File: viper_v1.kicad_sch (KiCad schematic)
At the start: 24 parts, among them SW1 SW_Push, SW2 SW_Push, SW3 SW_Push, SW4 SW_Push, SW5 SW_Push, U1 ATmega32U4-A, Y1 16MHz

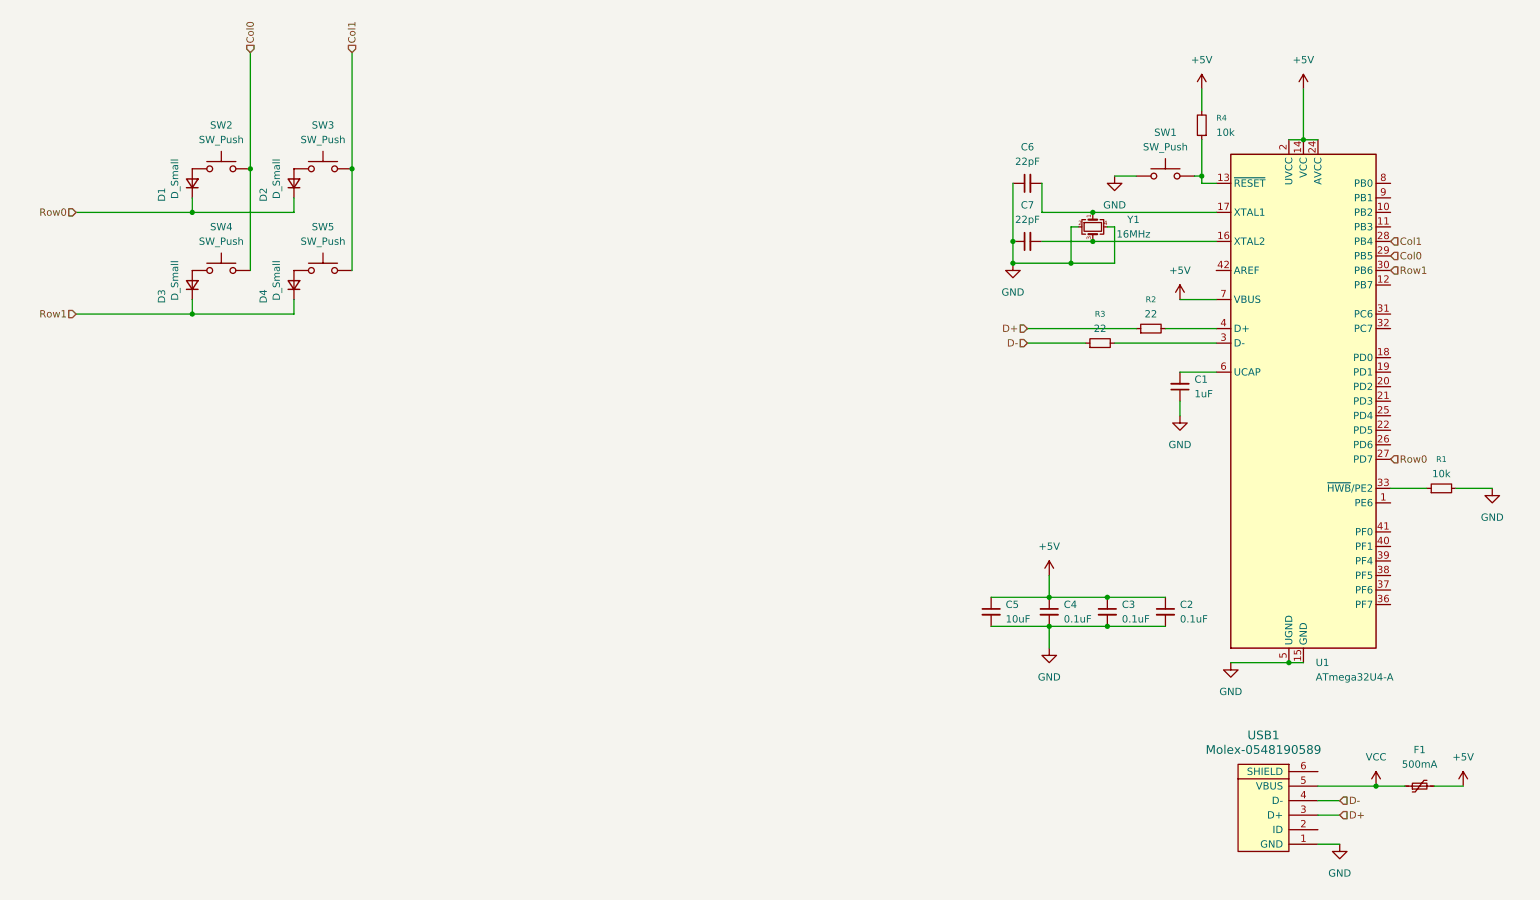
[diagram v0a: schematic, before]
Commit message: Assigned footprints
Updated/reannotated schematic

init pcb with viper outline

Add ISP header
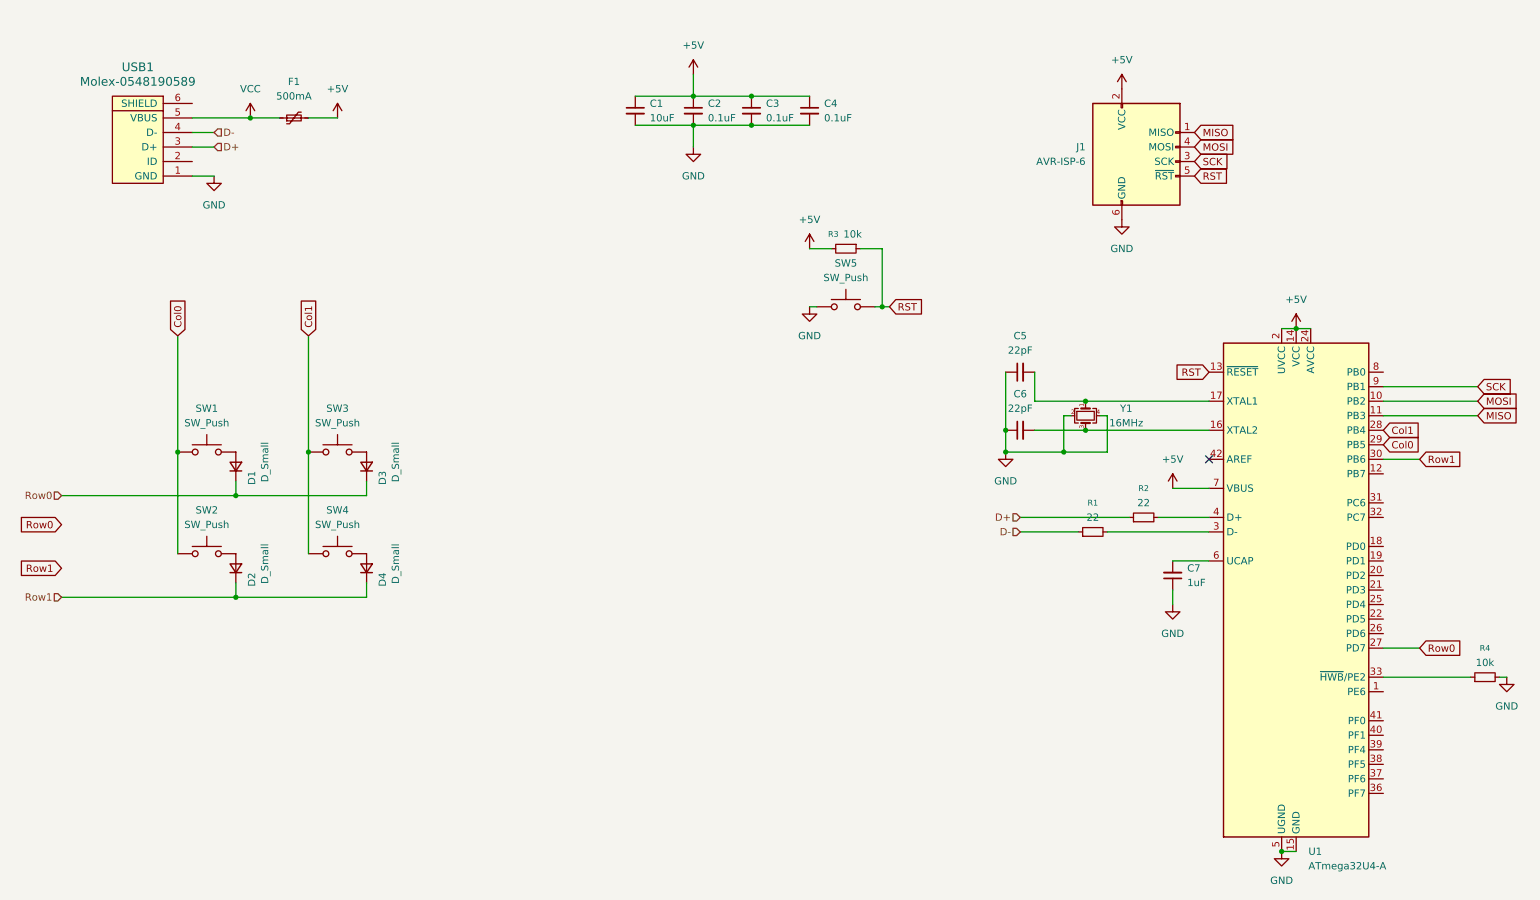
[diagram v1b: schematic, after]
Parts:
- removed SW5: SW_Push, symbol Switch:SW_Push
- added J1: AVR-ISP-6, random-keyboard-parts:Reset_Pretty-Mask, symbol Connector:AVR-ISP-6
- added SW1: SW_Push, MX_Solderable:MX-Solderable-1U, symbol Switch:SW_Push
- C1: renamed from C5; footprint (none) -> Capacitor_SMD:C_0805_2012Metric
- C2: renamed from C4; footprint (none) -> Capacitor_SMD:C_0805_2012Metric
- C3: footprint (none) -> Capacitor_SMD:C_0805_2012Metric
- C4: renamed from C2; footprint (none) -> Capacitor_SMD:C_0805_2012Metric
- C5: renamed from C6; footprint (none) -> Capacitor_SMD:C_0805_2012Metric
- C6: renamed from C7; footprint (none) -> Capacitor_SMD:C_0805_2012Metric
- C7: renamed from C1; footprint (none) -> Capacitor_SMD:C_0805_2012Metric
- D1, D2, D3, D4: footprint (none) -> Diode_SMD:D_SOD-123
- F1: footprint (none) -> Fuse:Fuse_1206_3216Metric
- R1: renamed from R3; footprint (none) -> Resistor_SMD:R_0805_2012Metric
- R2: footprint (none) -> Resistor_SMD:R_0805_2012Metric
- R3: renamed from R4; footprint (none) -> Resistor_SMD:R_0805_2012Metric
- R4: renamed from R1; footprint (none) -> Resistor_SMD:R_0805_2012Metric
- SW2, SW3, SW4: footprint (none) -> MX_Solderable:MX-Solderable-1U
- SW5: renamed from SW1; footprint (none) -> random-keyboard-parts:SKQG-1155865
- USB1: footprint (none) -> random-keyboard-parts:Molex-0548190589
- Y1: footprint (none) -> Crystal:Crystal_SMD_3225-4Pin_3.2x2.5mm
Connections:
- net +5V: now also J1.2 (VCC)
- net Col0: now also SW2.1, SW1.1; no longer SW2.2, SW4.2
- net Col1: now also SW3.1, SW4.1; no longer SW3.2
- net GND: now also J1.6 (GND)
- net Row0: now also D3.1 (K); no longer D2.1 (K)
- net Row1: now also D2.1 (K); no longer D3.1 (K)
- net RST: now reaches R3.1, SW5.2, U1.13 (~{RESET})
- net RST: now also J1.5 (~{RST})
- net at D1.2 (A): now also SW1.2; no longer SW2.1
- net at D4.2 (A): now also SW4.2
- net at D2.2 (A): now also SW2.2; no longer SW3.1
- net MOSI: now reaches U1.10 (PB2)
- net MOSI: now also J1.4 (MOSI)
- net MISO: now reaches U1.11 (PB3)
- net MISO: now also J1.1 (MISO)
- net SCK: now reaches U1.9 (PB1)
- net SCK: now also J1.3 (SCK)
- net at D3.2 (A): now also SW3.2; no longer SW4.1
- no-connect marks 0 -> 1
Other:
- moved on the sheet: C1, C2, C3, C4, C5, C6, C7, F1, R1, R2, R3, R4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

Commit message: Added rows/columns for simple wkl layout
Added values to keys in schematic & updated meta keys

Aligned switches & diodes

Moved some footprints around to prevent overlapping.

Added PWR Flags & connected shield

Custom SKQG footprint.

Set up 15mil power netclass for +5V, VCC & GND
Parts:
- removed D2: D_Small, Diode_SMD:D_SOD-123, symbol Device:D_Small
- removed SW2: SW_Push, MX_Solderable:MX-Solderable-1U, symbol Switch:SW_Push
- added D10, D11, D12, D13, D14, D15, D16, D17, D18, D19, D20, D21, D22, D23, D24, D25, D26, D27, D28, D29, D3, D30, D31, D32, D33, D34, D35, D36, D37, D38, D39, D40, D41, D42, D43, D44, D45, D46, D47, D48, D49, D5, D50, D51, D52, D53, D54, D55, D56, D57, D58, D6, D7, D8, D9: D_Small, Diode_SMD:D_SOD-123, symbol Device:D_Small
- added SW10: KC_9, MX_Solderable:MX-Solderable-1U, symbol Switch:SW_Push
- added SW11: KC_0, MX_Solderable:MX-Solderable-1U, symbol Switch:SW_Push
- added SW12: KC_MINS, MX_Solderable:MX-Solderable-1U, symbol Switch:SW_Push
- added SW13: KC_EQL, MX_Solderable:MX-Solderable-1U, symbol Switch:SW_Push
- added SW14: KC_BSPC, MX_Solderable:MX-Solderable-2U, symbol Switch:SW_Push
- added SW15: KC_TAB, MX_Solderable:MX-Solderable-1.5U, symbol Switch:SW_Push
- added SW16: KC_Q, MX_Solderable:MX-Solderable-1U, symbol Switch:SW_Push
- added SW17: KC_W, MX_Solderable:MX-Solderable-1U, symbol Switch:SW_Push
- added SW18: KC_E, MX_Solderable:MX-Solderable-1U, symbol Switch:SW_Push
- added SW19: KC_R, MX_Solderable:MX-Solderable-1U, symbol Switch:SW_Push
- added SW20: KC_T, MX_Solderable:MX-Solderable-1U, symbol Switch:SW_Push
- added SW21: KC_Y, MX_Solderable:MX-Solderable-1U, symbol Switch:SW_Push
- added SW22: KC_U, MX_Solderable:MX-Solderable-1U, symbol Switch:SW_Push
- added SW23: KC_I, MX_Solderable:MX-Solderable-1U, symbol Switch:SW_Push
- added SW24: KC_O, MX_Solderable:MX-Solderable-1U, symbol Switch:SW_Push
- added SW25: KC_P, MX_Solderable:MX-Solderable-1U, symbol Switch:SW_Push
- added SW26: KC_LBRC, MX_Solderable:MX-Solderable-1U, symbol Switch:SW_Push
- added SW27: KC_RBRC, MX_Solderable:MX-Solderable-1U, symbol Switch:SW_Push
- added SW28: KC_BSLS, MX_Solderable:MX-Solderable-1.5U, symbol Switch:SW_Push
- added SW29: KC_CAPS, MX_Solderable:MX-Solderable-1.75U, symbol Switch:SW_Push
- added SW3: KC_2, MX_Solderable:MX-Solderable-1U, symbol Switch:SW_Push
- added SW30: KC_A, MX_Solderable:MX-Solderable-1U, symbol Switch:SW_Push
- added SW31: KC_S, MX_Solderable:MX-Solderable-1U, symbol Switch:SW_Push
- added SW32: KC_D, MX_Solderable:MX-Solderable-1U, symbol Switch:SW_Push
- added SW33: KC_F, MX_Solderable:MX-Solderable-1U, symbol Switch:SW_Push
- added SW34: KC_G, MX_Solderable:MX-Solderable-1U, symbol Switch:SW_Push
- added SW35: KC_H, MX_Solderable:MX-Solderable-1U, symbol Switch:SW_Push
- added SW36: KC_J, MX_Solderable:MX-Solderable-1U, symbol Switch:SW_Push
- added SW37: KC_K, MX_Solderable:MX-Solderable-1U, symbol Switch:SW_Push
- added SW38: KC_L, MX_Solderable:MX-Solderable-1U, symbol Switch:SW_Push
- added SW39: KC_SCLN, MX_Solderable:MX-Solderable-1U, symbol Switch:SW_Push
- added SW40: KC_QUOT, MX_Solderable:MX-Solderable-1U, symbol Switch:SW_Push
- added SW41: KC_ENT, MX_Solderable:MX-Solderable-2.25U-ReversedStabilizers, symbol Switch:SW_Push
- added SW42: KC_LSFT, MX_Solderable:MX-Solderable-2.25U-ReversedStabilizers, symbol Switch:SW_Push
- added SW43: KC_Z, MX_Solderable:MX-Solderable-1U, symbol Switch:SW_Push
- added SW44: KC_X, MX_Solderable:MX-Solderable-1U, symbol Switch:SW_Push
- added SW45: KC_C, MX_Solderable:MX-Solderable-1U, symbol Switch:SW_Push
- added SW46: KC_V, MX_Solderable:MX-Solderable-1U, symbol Switch:SW_Push
- added SW47: KC_B, MX_Solderable:MX-Solderable-1U, symbol Switch:SW_Push
- added SW48: KC_N, MX_Solderable:MX-Solderable-1U, symbol Switch:SW_Push
- added SW49: KC_M, MX_Solderable:MX-Solderable-1U, symbol Switch:SW_Push
- added SW50: KC_COMM, MX_Solderable:MX-Solderable-1U, symbol Switch:SW_Push
- added SW51: KC_DOT, MX_Solderable:MX-Solderable-1U, symbol Switch:SW_Push
- added SW52: KC_SLSH, MX_Solderable:MX-Solderable-1U, symbol Switch:SW_Push
- added SW53: KC_RSFT, MX_Solderable:MX-Solderable-2.75U-ReversedStabilizers, symbol Switch:SW_Push
- added SW54: KC_LEFT_GUI, MX_Solderable:MX-Solderable-1U, symbol Switch:SW_Push
- added SW55: KC_LEFT_ALT, MX_Solderable:MX-Solderable-1.5U, symbol Switch:SW_Push
- added SW56: KC_SPACE, MX_Solderable:MX-Solderable-7U-ReversedStabilizers, symbol Switch:SW_Push
- added SW57: KC_RIGHT_GUI, MX_Solderable:MX-Solderable-1U, symbol Switch:SW_Push
- added SW58: KC_RIGHT_ALT, MX_Solderable:MX-Solderable-1.5U, symbol Switch:SW_Push
- added SW59: SW_RESET, random-keyboard-parts:SKQG-1155865, symbol Switch:SW_Push
- added SW6: KC_5, MX_Solderable:MX-Solderable-1U, symbol Switch:SW_Push
- added SW7: KC_6, MX_Solderable:MX-Solderable-1U, symbol Switch:SW_Push
- added SW8: KC_7, MX_Solderable:MX-Solderable-1U, symbol Switch:SW_Push
- added SW9: KC_8, MX_Solderable:MX-Solderable-1U, symbol Switch:SW_Push
- SW1: value SW_Push -> KC_GRV
- SW2: renamed from SW3; value SW_Push -> KC_1
- SW4: value SW_Push -> KC_3
- SW5: value SW_Push -> KC_4; footprint random-keyboard-parts:SKQG-1155865 -> MX_Solderable:MX-Solderable-1U
- renumbered D3 to D2, R3 to R1, R1 to R3
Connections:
- net Col0: now also U1.28 (PB4), SW15.1, SW29.1, SW42.1; no longer U1.29 (PB5)
- net Col1: now also U1.29 (PB5), SW16.1, SW30.1, SW54.1; no longer SW4.1, U1.28 (PB4)
- net GND: now also USB1.6 (SHIELD), SW59.1; no longer SW5.1
- net RST: now also SW59.2; no longer SW5.2
- net Row0: now also D4.1 (K), U1.1 (PE6), D10.1 (K), D11.1 (K), D12.1 (K), D13.1 (K), D14.1 (K), D3.1 (K), D5.1 (K), D6.1 (K), D7.1 (K), D8.1 (K), D9.1 (K); no longer U1.27 (PD7)
- net Row1: now also U1.38 (PF5), D15.1 (K), D16.1 (K), D17.1 (K), D18.1 (K), D19.1 (K), D20.1 (K), D21.1 (K), D22.1 (K), D23.1 (K), D24.1 (K), D25.1 (K), D26.1 (K), D27.1 (K), D28.1 (K); no longer D4.1 (K), U1.30 (PB6)
- net XTAL1: now reaches C5.2, U1.17 (XTAL1), Y1.1
- net XTAL2: now reaches C6.2, U1.16 (XTAL2), Y1.3
- net Col8: now reaches U1.19 (PD1)
- net Col8: now also SW23.1, SW37.1, SW49.1, SW9.1
- net Col9: now reaches U1.20 (PD2)
- net Col9: now also SW10.1, SW24.1, SW38.1, SW50.1
- net Col10: now reaches U1.21 (PD3)
- net Col10: now also SW11.1, SW25.1, SW39.1, SW51.1, SW57.1
- net Col11: now reaches U1.22 (PD5)
- net Col11: now also SW12.1, SW26.1, SW40.1, SW52.1, SW58.1
- net Col12: now reaches U1.25 (PD4)
- net Col12: now also SW13.1, SW27.1
- net Col13: now reaches U1.26 (PD6)
- net Col13: now also SW14.1, SW28.1, SW41.1, SW53.1
- net Col3: now reaches U1.31 (PC6)
- net Col3: now also SW4.1, SW18.1, SW32.1, SW44.1
- net Col4: now reaches U1.32 (PC7)
- net Col4: now also SW5.1, SW19.1, SW33.1, SW45.1
- net Col6: now reaches U1.36 (PF7)
- net Col6: now also SW21.1, SW35.1, SW47.1, SW56.1, SW7.1
- net Col5: now reaches U1.37 (PF6)
- net Col5: now also SW20.1, SW34.1, SW46.1, SW6.1
- net Row4: now reaches U1.39 (PF4)
- net Row4: now also D54.1 (K), D55.1 (K), D56.1 (K), D57.1 (K), D58.1 (K)
- net Row3: now reaches U1.40 (PF1)
- net Row3: now also D42.1 (K), D43.1 (K), D44.1 (K), D45.1 (K), D46.1 (K), D47.1 (K), D48.1 (K), D49.1 (K), D50.1 (K), D51.1 (K), D52.1 (K), D53.1 (K)
- net Row2: now reaches U1.41 (PF0)
- net Row2: now also D29.1 (K), D30.1 (K), D31.1 (K), D32.1 (K), D33.1 (K), D34.1 (K), D35.1 (K), D36.1 (K), D37.1 (K), D38.1 (K), D39.1 (K), D40.1 (K), D41.1 (K)
- net Col7: now reaches U1.8 (PB0)
- net Col7: now also SW22.1, SW36.1, SW48.1, SW8.1
- new net: D51.2 (A), SW51.2
- new net: D20.2 (A), SW20.2
- new net: D8.2 (A), SW8.2
- new net: D43.2 (A), SW43.2
- new net: D14.2 (A), SW14.2
- new net: D22.2 (A), SW22.2
- new net: D29.2 (A), SW29.2
- new net: D58.2 (A), SW58.2
- new net: D49.2 (A), SW49.2
- new net: D35.2 (A), SW35.2
- new net: D44.2 (A), SW44.2
- new net: D6.2 (A), SW6.2
- new net: D52.2 (A), SW52.2
- new net: D19.2 (A), SW19.2
- new net: D50.2 (A), SW50.2
- new net: D57.2 (A), SW57.2
- new net: D18.2 (A), SW18.2
- new net: D48.2 (A), SW48.2
- new net: D32.2 (A), SW32.2
- new net: D37.2 (A), SW37.2
- new net: D34.2 (A), SW34.2
- new net: D26.2 (A), SW26.2
- new net: D38.2 (A), SW38.2
- new net: D33.2 (A), SW33.2
- new net: D30.2 (A), SW30.2
- new net: D9.2 (A), SW9.2
- new net: D46.2 (A), SW46.2
- new net: D5.2 (A), SW5.2
- new net: D13.2 (A), SW13.2
- new net: D15.2 (A), SW15.2
- new net: D10.2 (A), SW10.2
- new net: D27.2 (A), SW27.2
- new net: D47.2 (A), SW47.2
- new net: D23.2 (A), SW23.2
- new net: D53.2 (A), SW53.2
- new net: D39.2 (A), SW39.2
- new net: D7.2 (A), SW7.2
- new net: D55.2 (A), SW55.2
- new net: D56.2 (A), SW56.2
- new net: D54.2 (A), SW54.2
- new net: D42.2 (A), SW42.2
- new net: D24.2 (A), SW24.2
- new net: D36.2 (A), SW36.2
- new net: D28.2 (A), SW28.2
- new net: D12.2 (A), SW12.2
- new net: D17.2 (A), SW17.2
- new net: D40.2 (A), SW40.2
- new net: D25.2 (A), SW25.2
- new net: D45.2 (A), SW45.2
- new net: D21.2 (A), SW21.2
- new net: D16.2 (A), SW16.2
- new net: D41.2 (A), SW41.2
- new net: D3.2 (A), SW3.2
- new net: D31.2 (A), SW31.2
- new net: D11.2 (A), SW11.2
- new net Col2: SW17.1, SW3.1, SW31.1, SW43.1, SW55.1, U1.30 (PB6)
- no-connect marks 1 -> 5
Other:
- moved on the sheet: C1, C2, C3, C4, C5, C6, C7, D1, D2, F1, J1, R1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

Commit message: Moved footprints to 0,0
Added better mounting holes

Testing different usb miniB footprints & replaced mounting holes.

Added another decoupling cap.

Reannotated parts

Centered diodes under switches where possible

Changed PCB edges around USB connector & added (optional) rounded corners.

45deg corners

Swapped rows/columns

Adding additional switch footprints.
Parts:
- removed USB1: Molex-0548190589, random-keyboard-parts:Molex-0548190589, symbol random-keyboard-parts:Molex-0548190589
- added C7: 0.1uF, Capacitor_SMD:C_0805_2012Metric, symbol Device:C_Small
- added D59, D60, D61: D_Small, Diode_SMD:D_SOD-123, symbol Device:D_Small
- added J1: USB_B_Mini, local:USB_miniB_hirose_5ST_hand, symbol Connector:USB_B_Mini
- added S1, S5, S6, S8, S9: Screw_Terminal_01x01, local:10x5_7x2.5mm, symbol Connector:Screw_Terminal_01x01
- added S2, S3, S4, S7: Screw_Terminal_01x01, local:5.5_5x2.5mm, symbol Connector:Screw_Terminal_01x01
- added SW60, SW61, SW62: KC_BSPC, MX_Solderable:MX-Solderable-2U, symbol Switch:SW_Push
- renumbered C5 to C1, C6 to C2, C1 to C3, C2 to C4, C3 to C5, C4 to C6, C7 to C8, J1 to J2, SW59 to SW1, SW9 to SW10, SW10 to SW11, SW11 to SW12, SW12 to SW13, SW13 to SW14, SW14 to SW15, SW15 to SW16, SW16 to SW17, SW17 to SW18, SW18 to SW19, SW1 to SW2, SW19 to SW20, SW20 to SW21, SW21 to SW22, SW22 to SW23, SW23 to SW24, SW24 to SW25, SW25 to SW26, SW26 to SW27, SW27 to SW28, SW28 to SW29, SW2 to SW3, SW29 to SW30, SW30 to SW31, SW31 to SW32, SW32 to SW33, SW33 to SW34, SW34 to SW35, SW35 to SW36, SW36 to SW37, SW37 to SW38, SW38 to SW39, SW3 to SW4, SW39 to SW40, SW40 to SW41, SW41 to SW42, SW42 to SW43, SW43 to SW44, SW44 to SW45, SW45 to SW46, SW46 to SW47, SW47 to SW48, SW48 to SW49, SW4 to SW5, SW49 to SW50, SW50 to SW51, SW51 to SW52, SW52 to SW53, SW53 to SW54, SW54 to SW55, SW55 to SW56, SW56 to SW57, SW57 to SW58, SW58 to SW59, SW5 to SW6, SW6 to SW7, SW7 to SW8, SW8 to SW9
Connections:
- net +5V: now also C7.1
- net Col0: now also SW16.2, SW2.2, SW30.2, SW43.2; no longer SW16.1, SW2.1, SW30.1, SW43.1
- net Col1: now also SW17.2, SW3.2, SW31.2, SW55.2; no longer SW17.1, SW3.1, SW31.1, SW55.1
- net Col10: now also SW12.2, SW26.2, SW40.2, SW52.2, SW58.2; no longer SW12.1, SW26.1, SW40.1, SW52.1, SW58.1
- net Col11: now also SW13.2, SW27.2, SW41.2, SW53.2, SW59.2; no longer SW13.1, SW27.1, SW41.1, SW53.1, SW59.1
- net Col12: now also SW14.2, SW28.2; no longer SW14.1, SW28.1
- net Col13: now also SW15.2, SW29.2, SW42.2, SW54.2; no longer SW15.1, SW29.1, SW42.1, SW54.1
- net Col2: now also SW18.2, SW32.2, SW4.2, SW44.2, SW56.2; no longer SW18.1, SW32.1, SW4.1, SW44.1, SW56.1
- net Col3: now also SW19.2, SW33.2, SW45.2, SW5.2; no longer SW19.1, SW33.1, SW45.1, SW5.1
- net Col4: now also SW20.2, SW34.2, SW46.2, SW6.2; no longer SW20.1, SW34.1, SW46.1, SW6.1
- net Col5: now also SW21.2, SW35.2, SW47.2, SW7.2; no longer SW21.1, SW35.1, SW47.1, SW7.1
- net Col6: now also SW22.2, SW36.2, SW48.2, SW57.2, SW8.2; no longer SW22.1, SW36.1, SW48.1, SW57.1, SW8.1
- net Col7: now also SW23.2, SW37.2, SW49.2, SW9.2; no longer SW23.1, SW37.1, SW49.1, SW9.1
- net Col8: now also SW10.2, SW24.2, SW38.2, SW50.2; no longer SW10.1, SW24.1, SW38.1, SW50.1
- net Col9: now also SW11.2, SW25.2, SW39.2, SW51.2; no longer SW11.1, SW25.1, SW39.1, SW51.1
- net D+: now also J1.3 (D+)
- net D-: now also J1.2 (D-)
- net GND: now also C7.2, J1.5 (GND), J1.6 (Shield), S1.1 (Pin_1), S2.1 (Pin_1), S3.1 (Pin_1), S4.1 (Pin_1), S5.1 (Pin_1), S6.1 (Pin_1), S7.1 (Pin_1), S8.1 (Pin_1), S9.1 (Pin_1)
- net VCC: now also J1.1 (VBUS)
- net at D51.2 (A): now also SW52.1; no longer SW52.2
- net at D20.2 (A): now also SW21.1; no longer SW21.2
- net at D8.2 (A): now also SW9.1; no longer SW9.2
- net at D43.2 (A): now also SW44.1; no longer SW44.2
- net at D14.2 (A): now also SW15.1; no longer SW15.2
- net at D22.2 (A): now also SW23.1; no longer SW23.2
- net at D29.2 (A): now also SW30.1; no longer SW30.2
- net at D58.2 (A): now also SW59.1; no longer SW59.2
- net at D49.2 (A): now also SW50.1; no longer SW50.2
- net at D35.2 (A): now also SW36.1; no longer SW36.2
- net at D44.2 (A): now also SW45.1; no longer SW45.2
- net at D6.2 (A): now also SW7.1; no longer SW7.2
- net at D52.2 (A): now also SW53.1; no longer SW53.2
- net at D19.2 (A): now also SW20.1; no longer SW20.2
- net at D4.2 (A): now also SW5.1; no longer SW5.2
- net at D50.2 (A): now also SW51.1; no longer SW51.2
- net at D57.2 (A): now also SW58.1; no longer SW58.2
- net at D18.2 (A): now also SW19.1; no longer SW19.2
- net at D48.2 (A): now also SW49.1; no longer SW49.2
- net at D32.2 (A): now also SW33.1; no longer SW33.2
- net at D37.2 (A): now also SW38.1; no longer SW38.2
- net at D34.2 (A): now also SW35.1; no longer SW35.2
- net at D26.2 (A): now also SW27.1; no longer SW27.2
- net at D38.2 (A): now also SW39.1; no longer SW39.2
- net at D33.2 (A): now also SW34.1; no longer SW34.2
- net at D30.2 (A): now also SW31.1; no longer SW31.2
- net at D9.2 (A): now also SW10.1; no longer SW10.2
- net at D1.2 (A): now also SW2.1; no longer SW2.2
- net at D46.2 (A): now also SW47.1; no longer SW47.2
- net at D5.2 (A): now also SW6.1; no longer SW6.2
- net at D13.2 (A): now also SW14.1; no longer SW14.2
- net at D15.2 (A): now also SW16.1; no longer SW16.2
- net at D10.2 (A): now also SW11.1; no longer SW11.2
- net at D27.2 (A): now also SW28.1; no longer SW28.2
- net at D47.2 (A): now also SW48.1; no longer SW48.2
- net at D23.2 (A): now also SW24.1; no longer SW24.2
- net at D53.2 (A): now also SW54.1; no longer SW54.2
- net at D39.2 (A): now also SW40.1; no longer SW40.2
- net at D7.2 (A): now also SW8.1; no longer SW8.2
- net at D55.2 (A): now also SW56.1; no longer SW56.2
- net at D56.2 (A): now also SW57.1; no longer SW57.2
- net at D54.2 (A): now also SW55.1; no longer SW55.2
- net at D2.2 (A): now also SW3.1; no longer SW3.2
- net at D42.2 (A): now also SW43.1; no longer SW43.2
- net at D24.2 (A): now also SW25.1; no longer SW25.2
- net at D36.2 (A): now also SW37.1; no longer SW37.2
- net at D28.2 (A): now also SW29.1; no longer SW29.2
- net at D12.2 (A): now also SW13.1; no longer SW13.2
- net at D17.2 (A): now also SW18.1; no longer SW18.2
- net at D40.2 (A): now also SW41.1; no longer SW41.2
- net at D25.2 (A): now also SW26.1; no longer SW26.2
- net at D45.2 (A): now also SW46.1; no longer SW46.2
- net at D21.2 (A): now also SW22.1; no longer SW22.2
- net at D16.2 (A): now also SW17.1; no longer SW17.2
- net at D41.2 (A): now also SW42.1; no longer SW42.2
- net at D3.2 (A): now also SW4.1; no longer SW4.2
- net at D31.2 (A): now also SW32.1; no longer SW32.2
- net at D11.2 (A): now also SW12.1; no longer SW12.2
- new net: D61.2 (A), SW62.1
- new net: D59.2 (A), SW60.1
- new net: D60.2 (A), SW61.1
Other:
- title: (none) -> Psyduck Viper
- moved on the sheet: C1, C2, C3, C4, C5, C6, C8, D1, D10, D11, D12, D13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
